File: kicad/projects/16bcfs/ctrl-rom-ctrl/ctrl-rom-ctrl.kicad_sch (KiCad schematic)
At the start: 70 parts, among them J1 Instruction, J2 Control ROM Address, J3 Raw Address for Pgm ROM, J4 Signal Header, J5 Power, J6 Power, U1 74HC08, U11 74HC157, U12 74HC157, U13 74HC157, U14 74HC157, U15 74HC193, U16 74HC193, U17 74HC193, U18 74HC193, U19 74HC04, U2 74HC74, U21 74HC08, U22 74HC08, U23 74HC32, U3 74HC03, U4 74HC193, U6 74HC00, U7 74HC00, U9 74HC165, X1 XO32

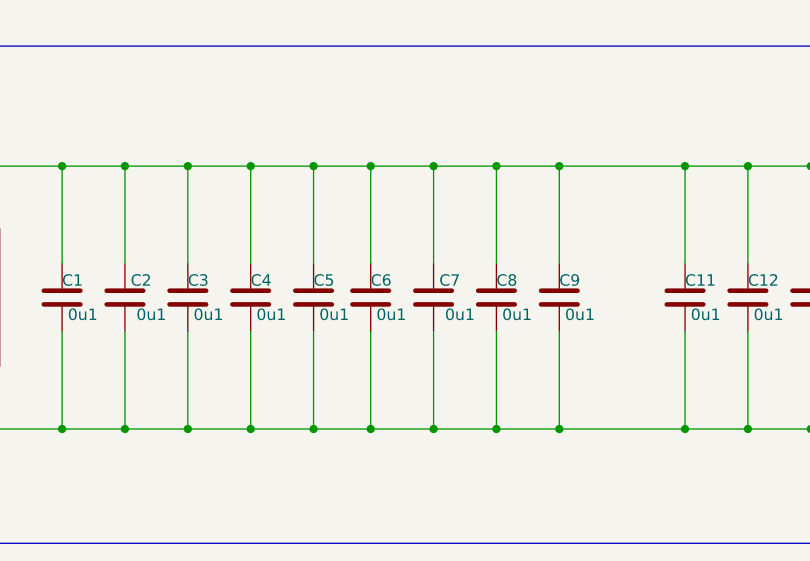
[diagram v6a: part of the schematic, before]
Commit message: Resolve the Control ROM Control pin alignment
This resulted in a major change to the PCB layout.
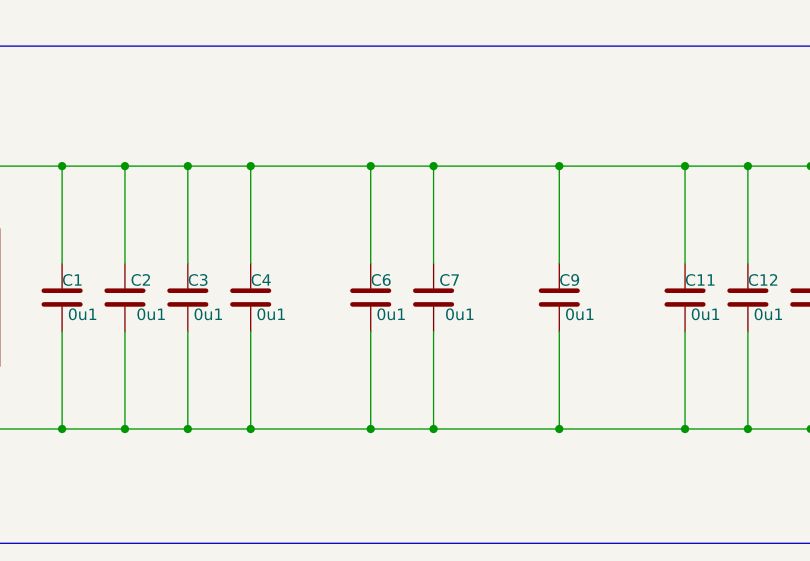
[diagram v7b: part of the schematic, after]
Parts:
- removed C5, C8: 0u1, Capacitor_SMD:C_1206_3216Metric_Pad1.33x1.80mm_HandSolder, symbol Device:C
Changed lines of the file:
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@@
   (junction (at 466.725 166.37) (diameter 0) (color 0 0 0 0)
   )
-  (junction (at 199.39 401.955) (diameter 0) (color 0 0 0 0)
-  )
   (junction (at 248.285 401.955) (diameter 0) (color 0 0 0 0)
   )
@@
   (junction (at 61.595 156.845) (diameter 0) (color 0 0 0 0)
   )
-  (junction (at 199.39 372.745) (diameter 0) (color 0 0 0 0)
-  )
   (junction (at 39.37 401.955) (diameter 0) (color 0 0 0 0)
   )
@@
   (junction (at 124.46 401.955) (diameter 0) (color 0 0 0 0)
   )
-  (junction (at 179.07 401.955) (diameter 0) (color 0 0 0 0)
-  )
   (junction (at 29.845 302.895) (diameter 0) (color 0 0 0 0)
   )
@@
   (junction (at 62.23 285.75) (diameter 0) (color 0 0 0 0)
   )
-  (junction (at 179.07 372.745) (diameter 0) (color 0 0 0 0)
-  )
   (junction (at 368.3 210.185) (diameter 0) (color 0 0 0 0)
   )
@@
     (stroke (width 0) (type default))
   )
-  (wire (pts (xy 199.39 372.745) (xy 192.405 372.745))
+  (wire (pts (xy 192.405 372.745) (xy 206.375 372.745))
     (stroke (width 0) (type default))
   )
@@
     (stroke (width 0) (type default))
   )
-  (wire (pts (xy 179.07 401.955) (xy 185.42 401.955))
+  (wire (pts (xy 172.085 401.955) (xy 185.42 401.955))
     (stroke (width 0) (type default))
   )
@@
     (stroke (width 0) (type default))
   )
-  (wire (pts (xy 179.07 372.745) (xy 179.07 383.54))
-    (stroke (width 0) (type default))
-  )
   (wire (pts (xy 291.465 93.345) (xy 293.37 93.345))
     (stroke (width 0) (type default))
@@
     (stroke (width 0) (type default))
   )
-  (wire (pts (xy 192.405 401.955) (xy 199.39 401.955))
+  (wire (pts (xy 192.405 401.955) (xy 206.375 401.955))
     (stroke (width 0) (type default))
   )
@@
     (stroke (width 0) (type default))
   )
-  (wire (pts (xy 199.39 372.745) (xy 206.375 372.745))
-    (stroke (width 0) (type default))
-  )
   (wire (pts (xy 206.375 372.745) (xy 220.345 372.745))
     (stroke (width 0) (type default))
@@
     (stroke (width 0) (type default))
   )
-  (wire (pts (xy 172.085 401.955) (xy 179.07 401.955))
-    (stroke (width 0) (type default))
-  )
   (wire (pts (xy 312.42 28.575) (xy 314.96 28.575))
     (stroke (width 0) (type default))
@@
     (stroke (width 0) (type default))
   )
-  (wire (pts (xy 199.39 391.16) (xy 199.39 401.955))
-    (stroke (width 0) (type default))
-  )
   (wire (pts (xy 368.3 215.265) (xy 372.745 215.265))
     (stroke (width 0) (type default))
@@
     (stroke (width 0) (type default))
   )
-  (wire (pts (xy 179.07 391.16) (xy 179.07 401.955))
-    (stroke (width 0) (type default))
-  )
   (wire (pts (xy 499.11 168.91) (xy 495.3 168.91))
     (stroke (width 0) (type default))
@@
     (stroke (width 0) (type default))
   )
-  (wire (pts (xy 199.39 372.745) (xy 199.39 383.54))
-    (stroke (width 0) (type default))
-  )
   (wire (pts (xy 515.62 64.77) (xy 515.62 67.945))
     (stroke (width 0) (type default))
@@
     (stroke (width 0) (type default))
   )
-  (wire (pts (xy 172.085 372.745) (xy 179.07 372.745))
-    (stroke (width 0) (type default))
-  )
   (wire (pts (xy 170.815 330.835) (xy 205.105 330.835))
     (stroke (width 0) (type default))
@@
     (stroke (width 0) (type default))
   )
-  (wire (pts (xy 199.39 401.955) (xy 206.375 401.955))
-    (stroke (width 0) (type default))
-  )
   (wire (pts (xy 454.66 346.075) (xy 464.185 346.075))
     (stroke (width 0) (type default))
@@
     (stroke (width 0) (type default))
   )
-  (wire (pts (xy 179.07 372.745) (xy 185.42 372.745))
+  (wire (pts (xy 172.085 372.745) (xy 185.42 372.745))
     (stroke (width 0) (type default))
   )
@@
     )
   )
-  (symbol (lib_id "Device:C") (at 179.07 387.35 0) (unit 1)
-    (in_bom yes) (on_board yes) (dnp no)
-    (property "Reference" "C5" (at 179.07 385.445 0)
-      (effects (font (size 1.27 1.27)) (justify left))
-    )
-    (property "Value" "0u1" (at 179.705 389.255 0)
-      (effects (font (size 1.27 1.27)) (justify left))
-    )
-    (property "Footprint" "Capacitor_SMD:C_1206_3216Metric_Pad1.33x1.80mm_HandSolder" (at 180.0352 391.16 0)
-      (effects (font (size 1.27 1.27)) hide)
-    )
-    (property "Datasheet" "~" (at 179.07 387.35 0)
-      (effects (font (size 1.27 1.27)) hide)
-    )
-    (pin "2")
-    (pin "1")
-    (instances
-      (project "ctrl-rom-ctrl"
-        (path "/d0ae44e5-d74e-4df6-bf3d-e0535c5a7785"
-          (reference "C5") (unit 1)
-        )
-      )
-    )
-  )
   (symbol (lib_id "74xx:74HC00") (at 127.635 139.065 0) (mirror x) (unit 4)
     (in_bom yes) (on_board yes) (dnp no)
@@
         )
       )
-    )
-  )
-  (symbol (lib_id "Device:C") (at 199.39 387.35 0) (unit 1)
-    (in_bom yes) (on_board yes) (dnp no)
-    (property "Reference" "C8" (at 199.39 385.445 0)
-      (effects (font (size 1.27 1.27)) (justify left))
-    )
-    (property "Value" "0u1" (at 200.025 389.255 0)
-      (effects (font (size 1.27 1.27)) (justify left))
-    )
-    (property "Footprint" "Capacitor_SMD:C_1206_3216Metric_Pad1.33x1.80mm_HandSolder" (at 200.3552 391.16 0)
-      (effects (font (size 1.27 1.27)) hide)
-    )
-    (property "Datasheet" "~" (at 199.39 387.35 0)
-      (effects (font (size 1.27 1.27)) hide)
-    )
-    (pin "2")
-    (pin "1")
-    (instances
-      (project "ctrl-rom-ctrl"
-        (path "/d0ae44e5-d74e-4df6-bf3d-e0535c5a7785"
-          (reference "C8") (unit 1)
-        )
-      )

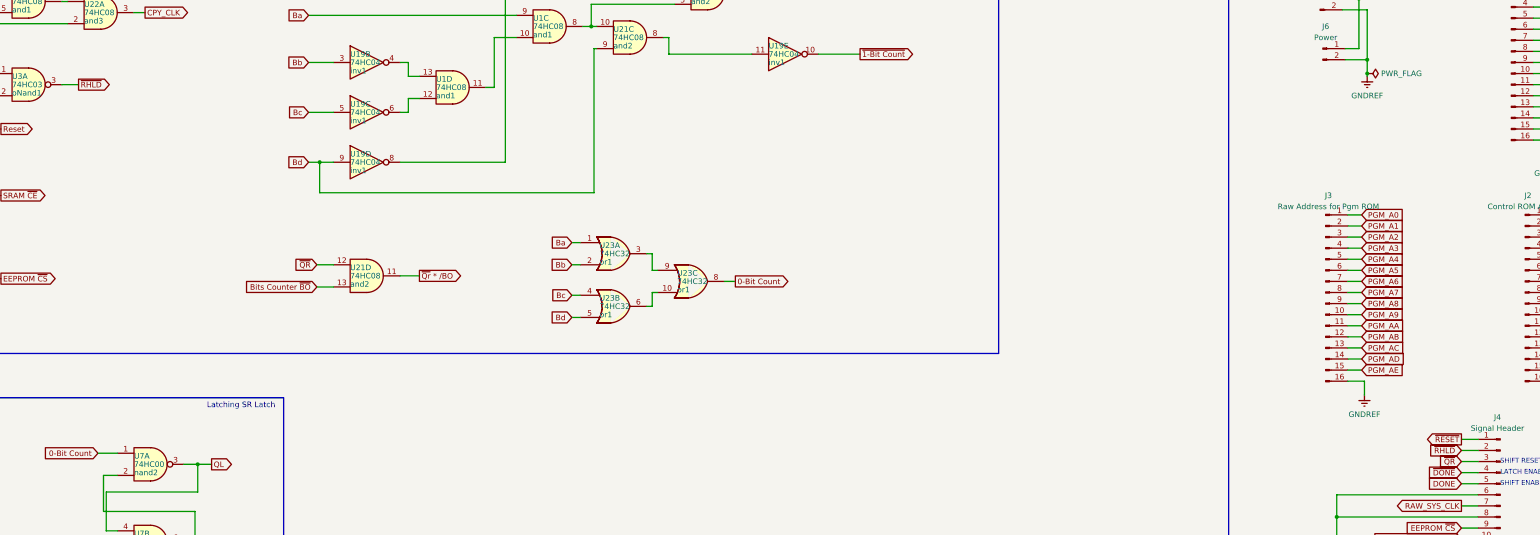
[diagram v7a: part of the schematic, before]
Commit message: Rename #RHLD to #CPYHLD on the Ctrl Rom Ctrl & Midplane
The logic for the signal does not change, but the purpose does.  The
Reset Circuit will handle the #RHLD now, but it needs to know when the
copy is complete.
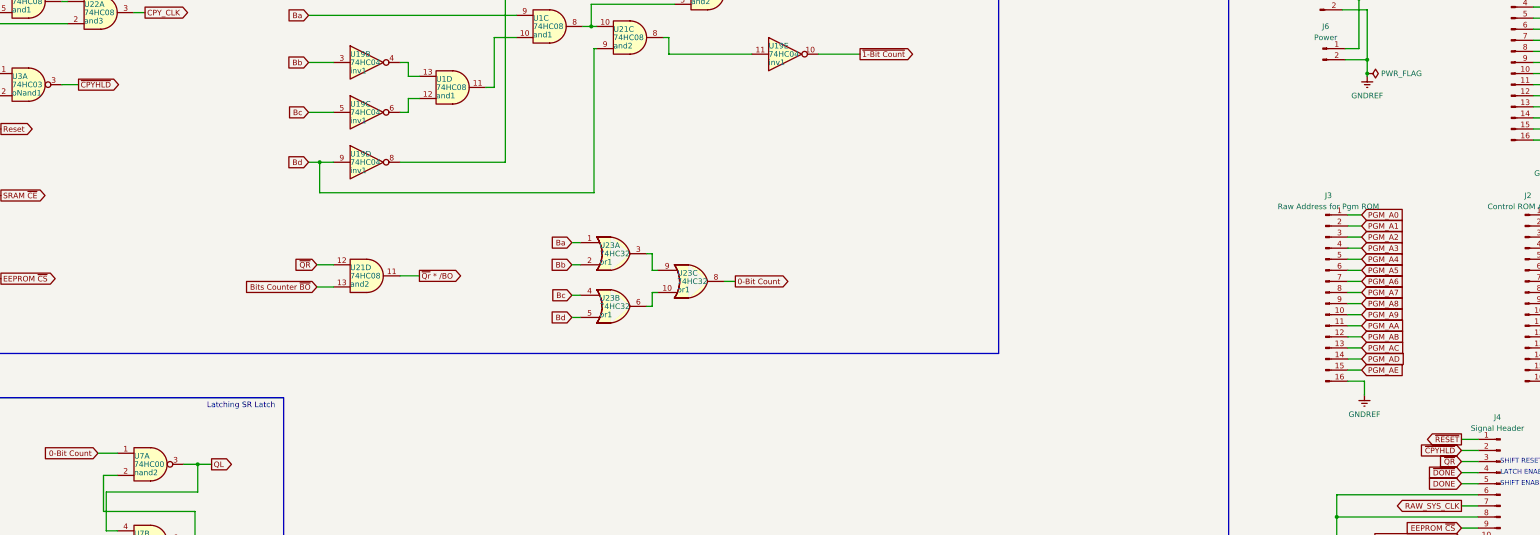
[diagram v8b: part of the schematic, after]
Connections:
- net ~{RHLD} renamed ~{CPYHLD}
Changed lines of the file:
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@@
     )
   )
-  (global_label "~{RHLD}" (shape output) (at 178.435 52.07 0) (fields_autoplaced)
-    (effects (font (size 1.27 1.27)) (justify left))
-    (property "Intersheetrefs" "${INTERSHEET_REFS}" (at 186.3188 52.07 0)
+  (global_label "~{CPYHLD}" (shape output) (at 178.435 52.07 0) (fields_autoplaced)
+    (effects (font (size 1.27 1.27)) (justify left))
+    (property "Intersheetrefs" "${INTERSHEET_REFS}" (at 188.6774 52.07 0)
       (effects (font (size 1.27 1.27)) (justify left) hide)
     )
@@
     )
   )
-  (global_label "~{RHLD}" (shape input) (at 495.3 135.89 180) (fields_autoplaced)
-    (effects (font (size 1.27 1.27)) (justify right))
-    (property "Intersheetrefs" "${INTERSHEET_REFS}" (at 487.4162 135.89 0)
-      (effects (font (size 1.27 1.27)) (justify right) hide)
-    )
+  (global_label "~{CPYHLD}" (shape input) (at 495.3 135.89 180) (fields_autoplaced)
+    (effects (font (size 1.27 1.27)) (justify right))
+    (property "Intersheetrefs" "${INTERSHEET_REFS}" (at 485.0576 135.89 0)
+      (effects (font (size 1.27 1.27)) (justify right) hide)
+    )
